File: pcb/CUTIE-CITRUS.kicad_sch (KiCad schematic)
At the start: 0 parts

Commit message: added xc7z020clg484 symbol and hierarchy
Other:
- added sheet Backplane Connector (backplane.kicad_sch)
- added sheet Zynq (soc.kicad_sch)
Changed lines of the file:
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@@
 	(generator_version "9.0")
 	(paper "A4")
+	(sheet
+		(at 91.44 137.16)
+		(size 50.8 35.56)
+		(exclude_from_sim no)
+		(in_bom yes)
+		(on_board yes)
+		(dnp no)
+		(fields_autoplaced yes)
+		(stroke
+			(width 0.1524)
+			(type solid)
+		)
+		(fill
+			(color 0 0 0 0.0000)
+		)
+		(property "Sheetname" "Backplane Connector"
+			(at 91.44 136.4484 0)
+			(effects
+				(font
+					(size 1.27 1.27)
+				)
+				(justify left bottom)
+			)
+		)
+		(property "Sheetfile" "backplane.kicad_sch"
+			(at 91.44 173.3046 0)
+			(effects
+				(font
+					(size 1.27 1.27)
+				)
+				(justify left top)
+			)
+		)
+		(instances
+			(project "CUTIE-CITRUS"
+				(path "/875da261-7543-41df-9bd5-25bca104c872"
+					(page "4")
+				)
+			)
+		)
+	)
+	(sheet
+		(at 127 81.28)
+		(size 20.32 35.56)
+		(exclude_from_sim no)
+		(in_bom yes)
+		(on_board yes)
+		(dnp no)
+		(fields_autoplaced yes)
+		(stroke
+			(width 0.1524)
+			(type solid)
+		)
+		(fill
+			(color 194 0 194 0.0600)
+		)
+		(property "Sheetname" "Zynq"
+			(at 127 80.5684 0)
+			(effects
+				(font
+					(size 1.27 1.27)
+				)
+				(justify left bottom)
+			)
+		)
+		(property "Sheetfile" "soc.kicad_sch"
+			(at 127 117.4246 0)
+			(effects
+				(font
+					(size 1.27 1.27)
+				)
+				(justify left top)
+			)
+		)
+		(instances
+			(project "CUTIE-CITRUS"
+				(path "/875da261-7543-41df-9bd5-25bca104c872"
+					(page "2")
+				)
+			)
+		)
+	)
 	(sheet_instances
 		(path "/"

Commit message: hierarchy and cleaning
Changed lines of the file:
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@@
 	(paper "A4")
 	(sheet
-		(at 91.44 137.16)
-		(size 50.8 35.56)
+		(at 71.12 137.16)
+		(size 63.5 15.24)
 		(exclude_from_sim no)
 		(in_bom yes)
@@
 		)
 		(property "Sheetname" "Backplane Connector"
-			(at 91.44 136.4484 0)
+			(at 71.12 136.4484 0)
 			(effects
 				(font
@@
 		)
 		(property "Sheetfile" "backplane.kicad_sch"
-			(at 91.44 173.3046 0)
+			(at 71.12 152.9846 0)
 			(effects
 				(font

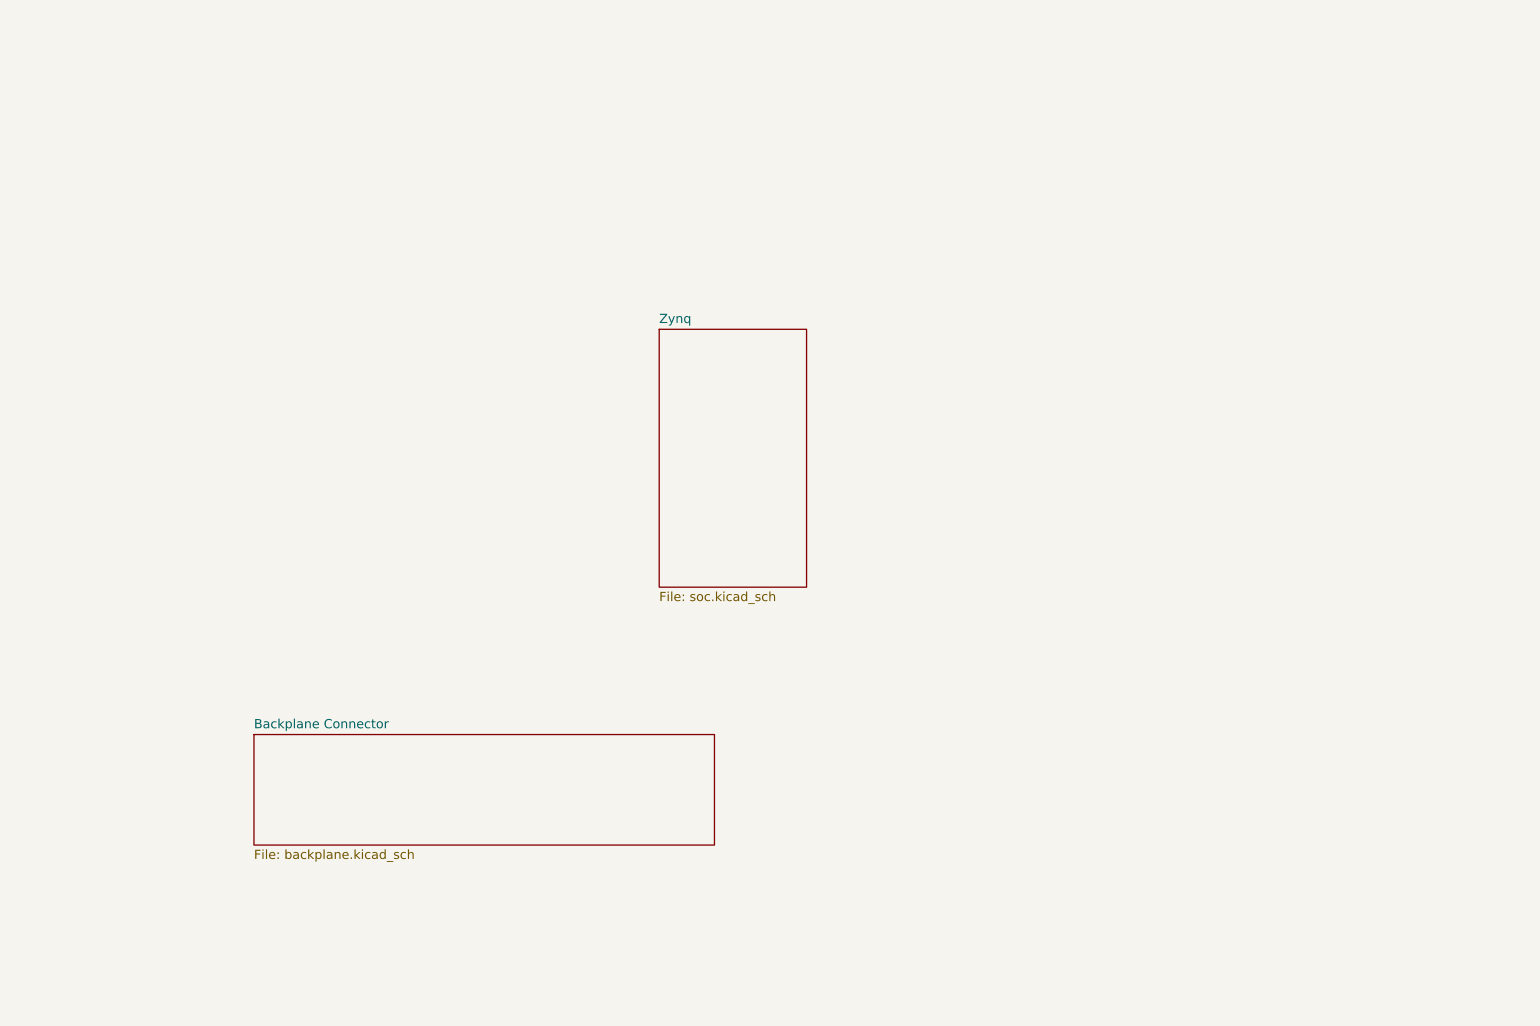
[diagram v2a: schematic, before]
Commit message: schematic structure, added qspi flash, pinout defs. mostly work on PS pinouts, defining comms. buses, still need to choose dram part, phys, camera/bus, power supply etc
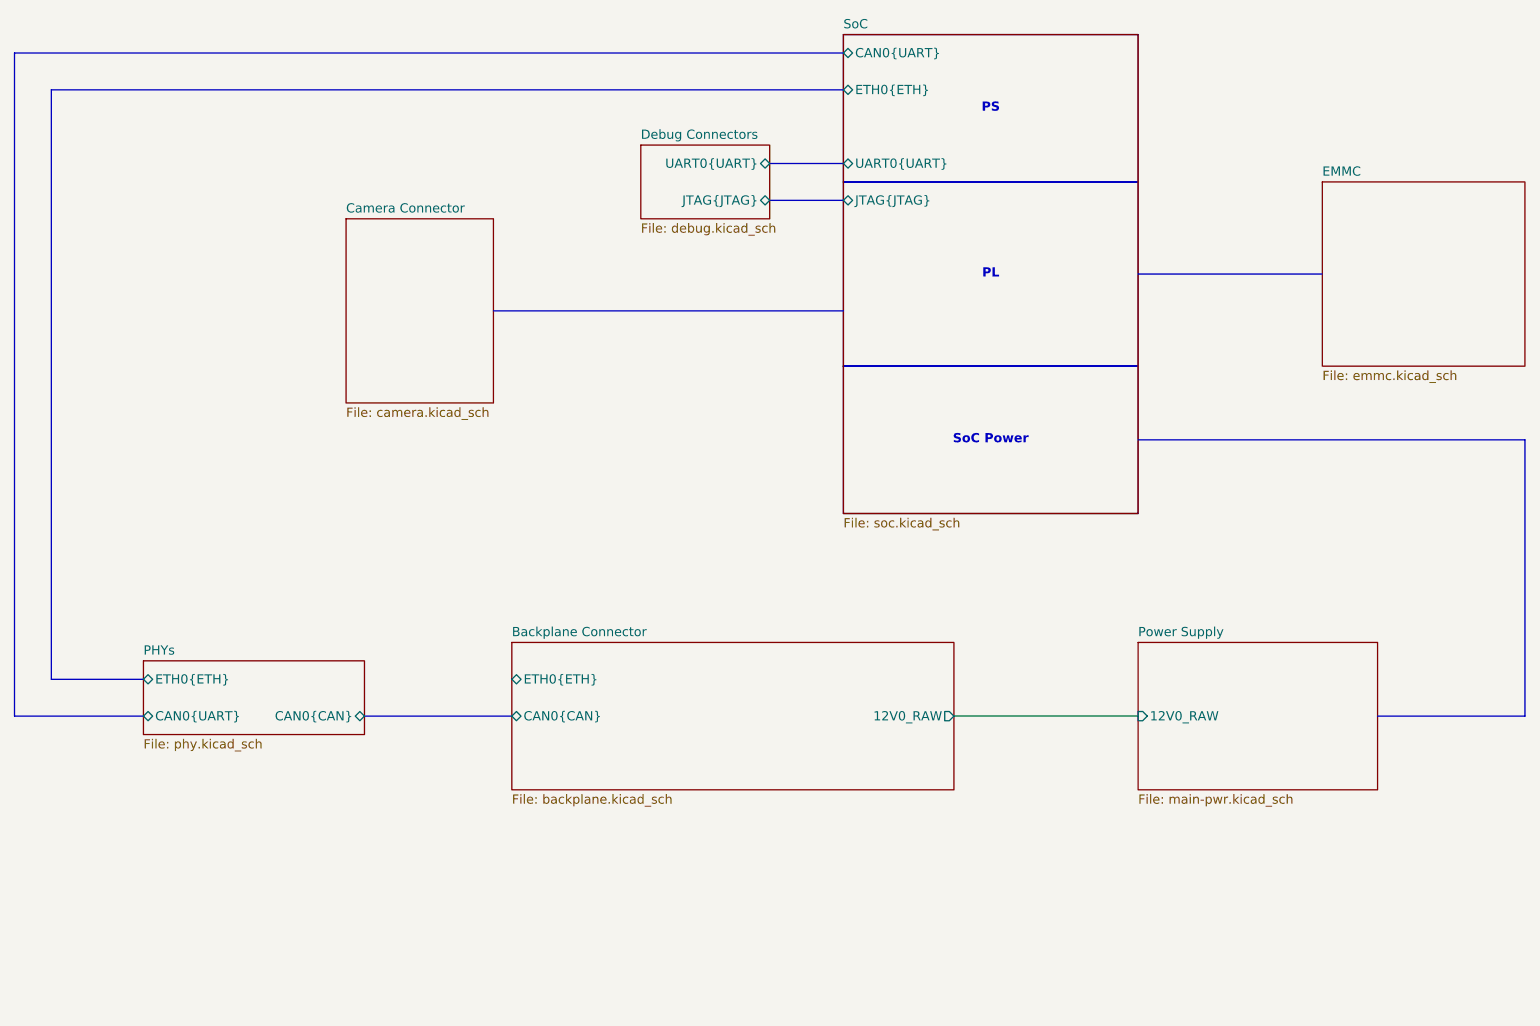
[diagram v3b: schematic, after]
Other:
- sheet Zynq renamed SoC
- added sheet Camera Connector (camera.kicad_sch)
- added sheet Debug Connectors (debug.kicad_sch)
- added sheet EMMC (emmc.kicad_sch)
- added sheet PHYs (phy.kicad_sch)
- added sheet Power Supply (main-pwr.kicad_sch)
- sheet Backplane Connector ports: added 12V0_RAW, CAN0{CAN}, ETH0{ETH}; removed none
- sheet SoC ports: added CAN0{UART}, ETH0{ETH}, JTAG{JTAG}, UART0{UART}; removed none
- note added: "PL"
- note added: "PS"
- note added: "SoC Power"
- company: (none) -> Andre S Winkel | Highlander Space Program
- title: (none) -> CUTIE-CITRUS

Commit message: edits to eth0 protocol names / bus aliases
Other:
- sheet Backplane Connector ports: added ETH0{MDI}; removed ETH0{ETH}
- sheet PHYs ports: added ETH0{MDI}, ETH0{RGMII}; removed ETH0{ETH}
- sheet SoC ports: added ETH0{RGMII}; removed ETH0{ETH}
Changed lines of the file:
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@@
 		(company "Andre S Winkel | Highlander Space Program")
+	)
+	(bus_alias "MDI"
+		(members "0_P" "0_N" "1_P" "1_N" "2_P" "2_N" "3_P" "3_N")
 	)
 	(rectangle
@@
 	(bus
 		(pts
+			(xy 86.36 129.54) (xy 106.68 129.54)
+		)
+		(stroke
+			(width 0)
+			(type default)
+		)
+	)
+	(bus
+		(pts
 			(xy 246.38 134.62) (xy 246.38 96.52)
 		)
@@
 			)
 		)
-		(pin "ETH0{ETH}" bidirectional
+		(pin "ETH0{MDI}" bidirectional
 			(at 106.68 129.54 180)
 			(effects
@@
 			)
 		)
-		(pin "ETH0{ETH}" bidirectional
+		(pin "ETH0{RGMII}" bidirectional
 			(at 55.88 129.54 180)
 			(effects
@@
 				)
 				(justify left)
+			)
+		)
+		(pin "ETH0{MDI}" bidirectional
+			(at 86.36 129.54 0)
+			(effects
+				(font
+					(size 1.27 1.27)
+				)
+				(justify right)
 			)
 		)
@@
 			)
 		)
-		(pin "ETH0{ETH}" bidirectional
+		(pin "ETH0{RGMII}" bidirectional
 			(at 152.4 48.26 180)
 			(effects

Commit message: add eth phy
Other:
- sheet SoC ports: added 1V0_FD, 1V35_DDR, 1V8_FD, 3V3_FD; removed none
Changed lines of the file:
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@@
-	(bus
-		(pts
-			(xy 246.38 134.62) (xy 246.38 96.52)
-		)
-		(stroke
-			(width 0)
-			(type default)
-		)
-	)
 	(bus
 		(pts
@@
 		)
 	)
-	(bus
-		(pts
-			(xy 226.06 134.62) (xy 246.38 134.62)
-		)
-		(stroke
-			(width 0)
-			(type default)
-		)
-	)
 	(wire
 		(pts
@@
 		(pts
 			(xy 152.4 43.18) (xy 38.1 43.18)
-		)
-		(stroke
-			(width 0)
-			(type default)
-		)
-	)
-	(bus
-		(pts
-			(xy 193.04 96.52) (xy 246.38 96.52)
 		)
 		(stroke
@@
 			)
 		)
+		(pin "1V0_FD" input
+			(at 193.04 91.44 0)
+			(effects
+				(font
+					(size 1.27 1.27)
+				)
+				(justify right)
+			)
+		)
+		(pin "1V8_FD" input
+			(at 193.04 96.52 0)
+			(effects
+				(font
+					(size 1.27 1.27)
+				)
+				(justify right)
+			)
+		)
+		(pin "1V35_DDR" input
+			(at 193.04 93.98 0)
+			(effects
+				(font
+					(size 1.27 1.27)
+				)
+				(justify right)
+			)
+		)
+		(pin "3V3_FD" input
+			(at 193.04 101.6 0)
+			(effects
+				(font
+					(size 1.27 1.27)
+				)
+				(justify right)
+			)
+		)
